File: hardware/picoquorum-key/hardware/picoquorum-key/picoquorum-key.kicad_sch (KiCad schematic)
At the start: 52 parts, among them J1 USB-C, J2 ST7789 1.14in panel, Q1 AO3401A, Q2 MMBT3904, SW1 D0 Reject, SW2 D1 Next, SW3 D2 Sign, SW6 BOOT, SW7 RESET, U1 ESP32-S3-WROOM-1-N8R2, U2 ATECC608C-MAHDA, U3 AMS1117-3.3, U4 USBLC6-2SC6

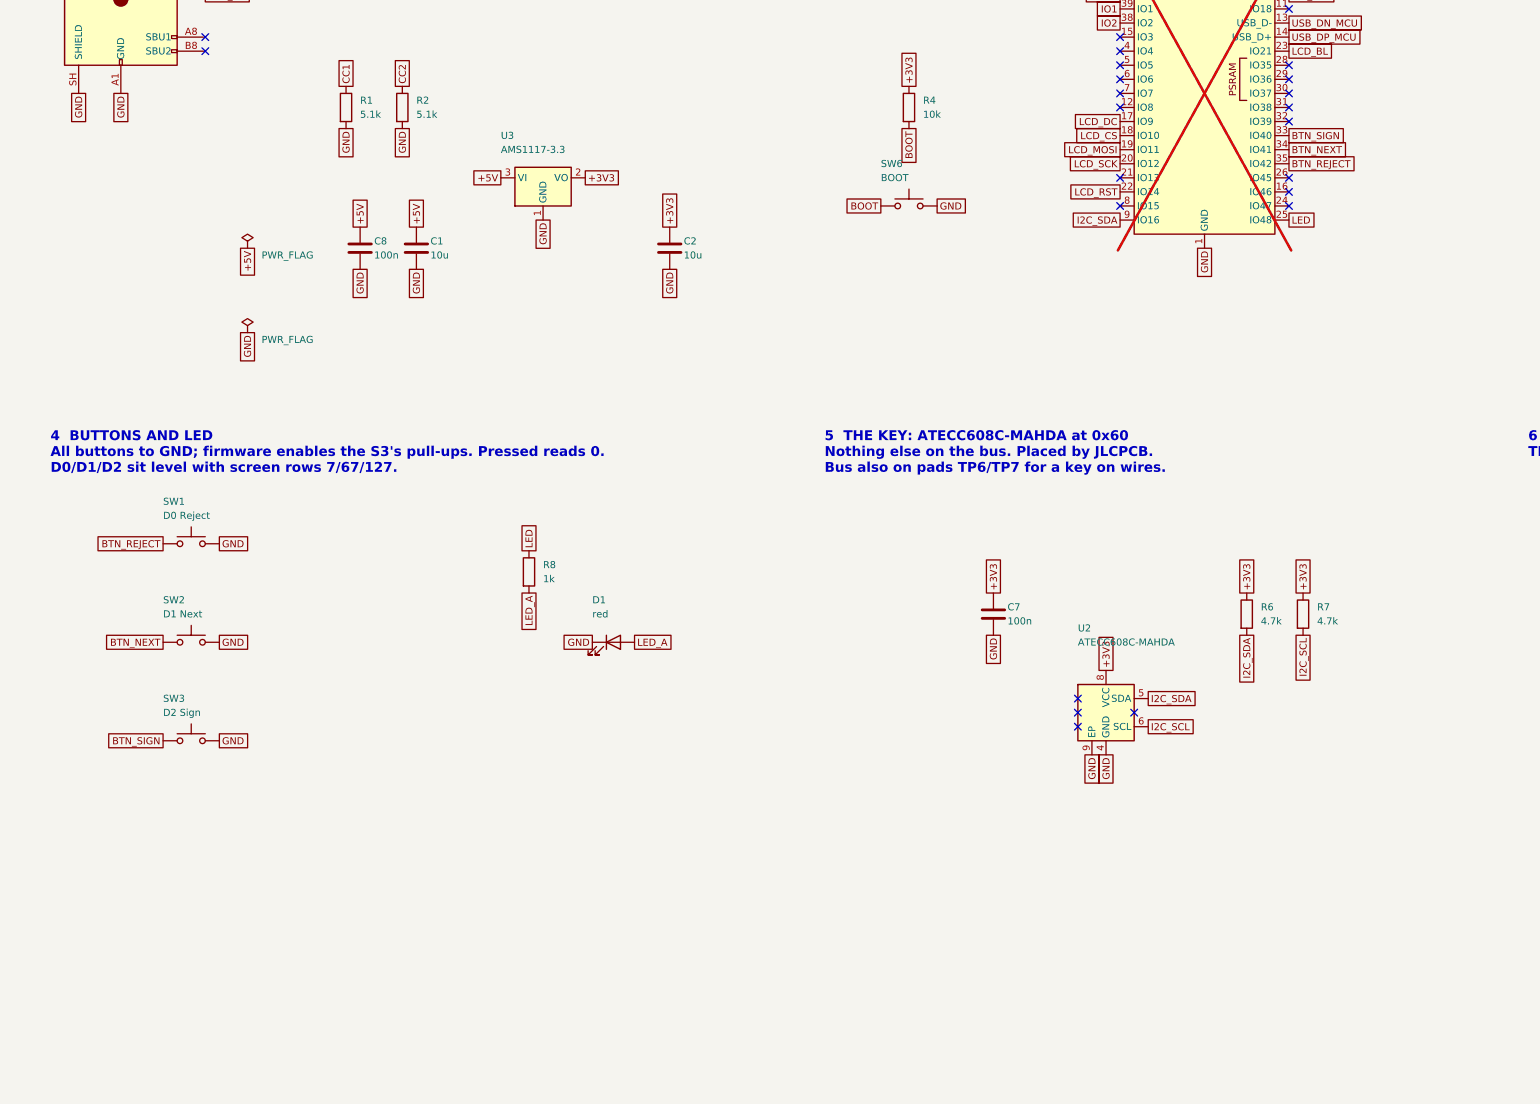
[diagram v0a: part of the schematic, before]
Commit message: picoquorum-key: an optional key port, a right-angle USB-C plug for key-c
Pads on the back for an HRO TYPE-C-31-G-03 plug at the left edge, beside the
module, its body past the edge, and its parts beside it: an AP22653 switch for
the key's power (80 mA, reverse blocking, IO2 enables it), SRV05-4 ESD on SDA,
SCL and CC, a TVS on VKEY, 2.2k pull-ups to VKEY, and CC on IO1 through a 22k
pull-up, so a key in reads 0.62 V (a logic low) and a swap shows as two edges.
The plugged key gets its own bus, IO39/IO38, since it and U2 both answer at
0x60.

Every port part is DNP: bom.csv and cpl.csv are byte for byte as before, and
unfitted the board behaves as rev A did. The console image doesn't use the port
yet; that is a firmware change and a new release.

The plug's escape is drawn and locked by gen_pcb.py. The board was routed
again (DESIGN.md, Routing): DRC, ERC and parity clean, USB skew 8.7 mm.
post_route.py no longer stacks a stitching via on an existing one. The back's
title text moved to make room. tools/test.sh: 125 tests pass, 11 skipped (no
FreeCAD here); golden images re-approved after checking the diffs.

Co-Authored-By: Claude Opus 5.5 <noreply@anthropic.com>
Claude-Session: https://claude.ai/code/session_01F8ny43JrASLAVMDnk3ynk2
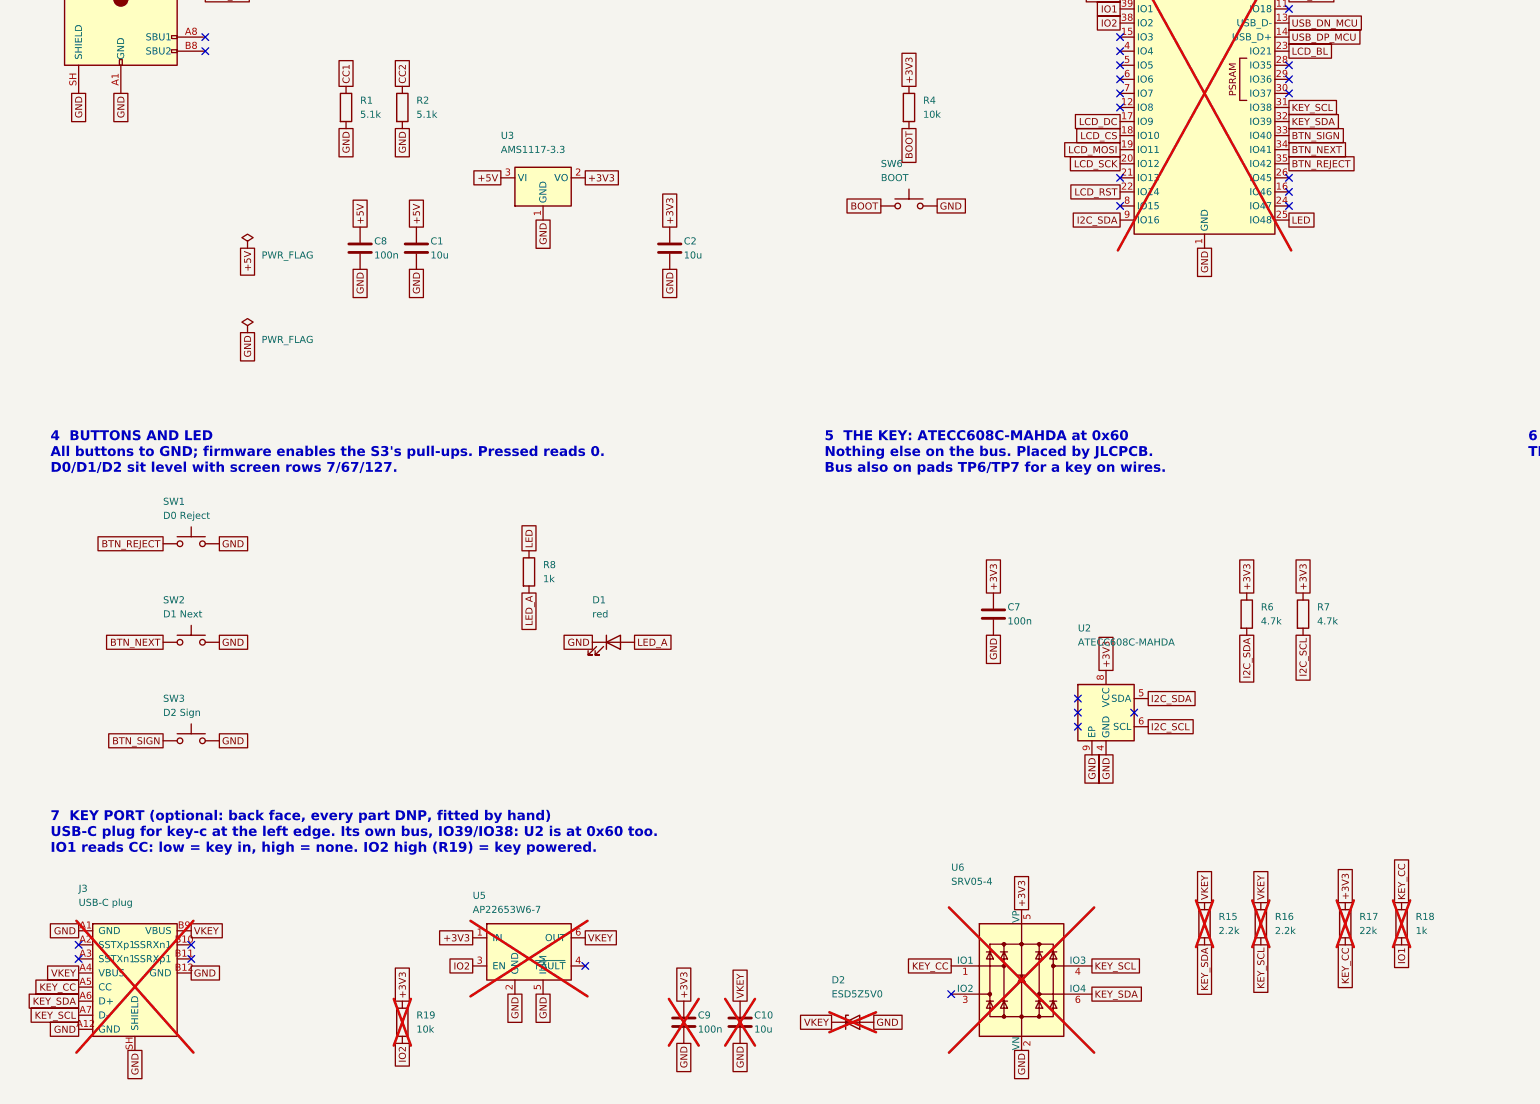
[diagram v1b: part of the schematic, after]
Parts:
- added C10: 10u, Capacitor_SMD:C_0805_2012Metric, symbol Device:C
- added C9: 100n, Capacitor_SMD:C_0603_1608Metric, symbol Device:C
- added D2: ESD5Z5V0, Diode_SMD:D_SOD-523, symbol Diode:ESD5Zxx
- added J3: USB-C plug, console:USB_C_Plug_HRO_TYPE-C-31-G-03_Edge, symbol console:USB_C_Plug_12P
- added R15, R16: 2.2k, Resistor_SMD:R_0603_1608Metric, symbol Device:R
- added R17: 22k, Resistor_SMD:R_0603_1608Metric, symbol Device:R
- added R18: 1k, Resistor_SMD:R_0603_1608Metric, symbol Device:R
- added R19: 10k, Resistor_SMD:R_0603_1608Metric, symbol Device:R
- added U5: AP22653W6-7, Package_TO_SOT_SMD:SOT-23-6, symbol console:AP22653
- added U6: SRV05-4, Package_TO_SOT_SMD:SOT-23-6, symbol Power_Protection:SRV05-4
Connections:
- net +3V3: now also C9.1, R17.1, R19.1, U5.1 (IN), U6.5 (VP)
- net GND: now also C10.2, C9.2, D2.2 (A), J3.A1 (GND), J3.A12 (GND), J3.B12 (GND), J3.SH (SHIELD), U5.2 (GND), U5.5 (ILIM), U6.2 (VN)
- net IO1: now also R18.2
- net IO2: now also R19.2, U5.3 (EN)
- net KEY_SCL: now reaches U1.31 (IO38)
- net KEY_SCL: now also J3.A7 (D-), R16.2, U6.4 (IO3)
- net KEY_SDA: now reaches U1.32 (IO39)
- net KEY_SDA: now also J3.A6 (D+), R15.2, U6.6 (IO4)
- new net KEY_CC: J3.A5 (CC), R17.2, R18.1, U6.1 (IO1)
- new net VKEY: C10.1, D2.1 (K), J3.A4 (VBUS), J3.B9 (VBUS), R15.1, R16.1, U5.6 (OUT)
- no-connect marks 23 -> 27
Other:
- note added: "7 KEY PORT (optional: back face, every part DNP, fitted by hand) USB-C plug for key-c at the left edge. Its own bus, IO39/IO38: U2 is at 0x60 too. IO1 reads CC: low = key in, high = none. IO2 high (R19) = key powered."
